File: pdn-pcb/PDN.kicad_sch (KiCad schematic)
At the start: 22 parts, among them CN1 PH-3AW_C722773, CN10 PH-6AW_C722785, CN2 PH-3AW_C722773, CN3 PH-4AW_C722777, CN4 PH-4AW_C722777, CN5 PH-3AW_C722773, CN6 PH-4AW_C722777, CN7 PH-4AW_C722777, CN8 PH-6AW_C722785, CN9 PH-3AW_C722773

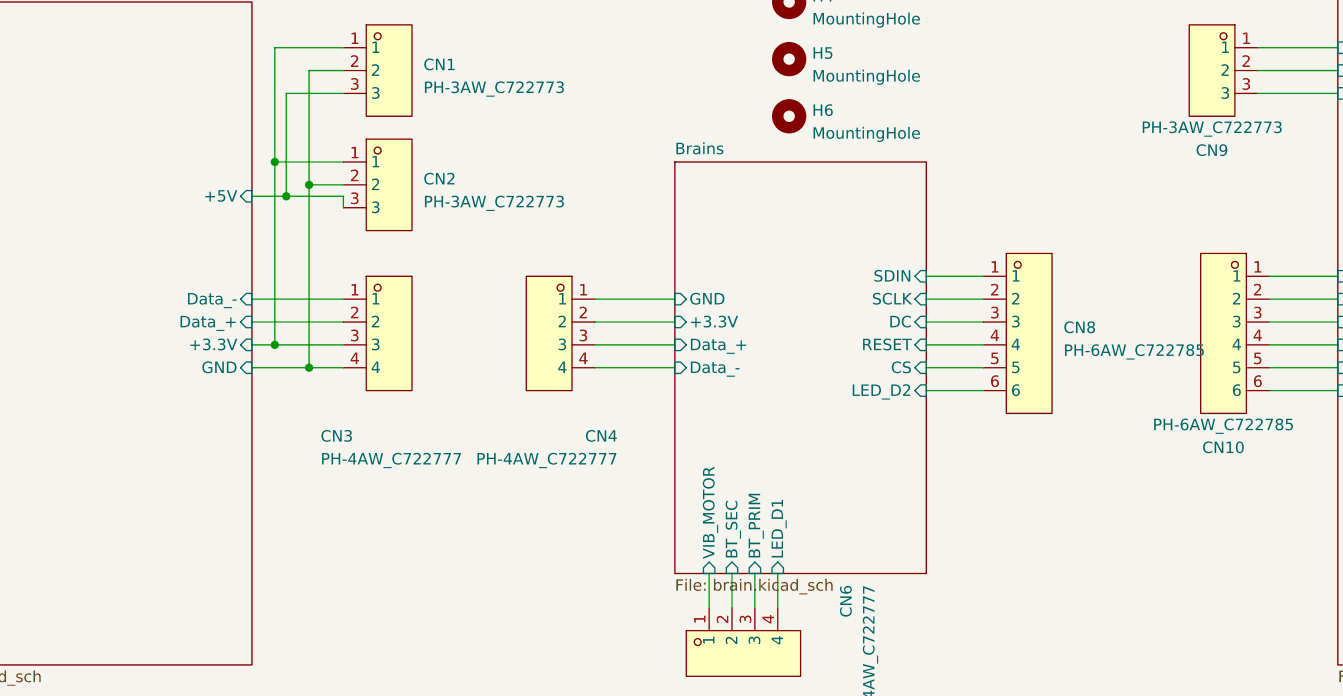
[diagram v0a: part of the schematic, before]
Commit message: Updated 3v3 LDO to an LDL1117, reworked the brain board and added TVS protection.
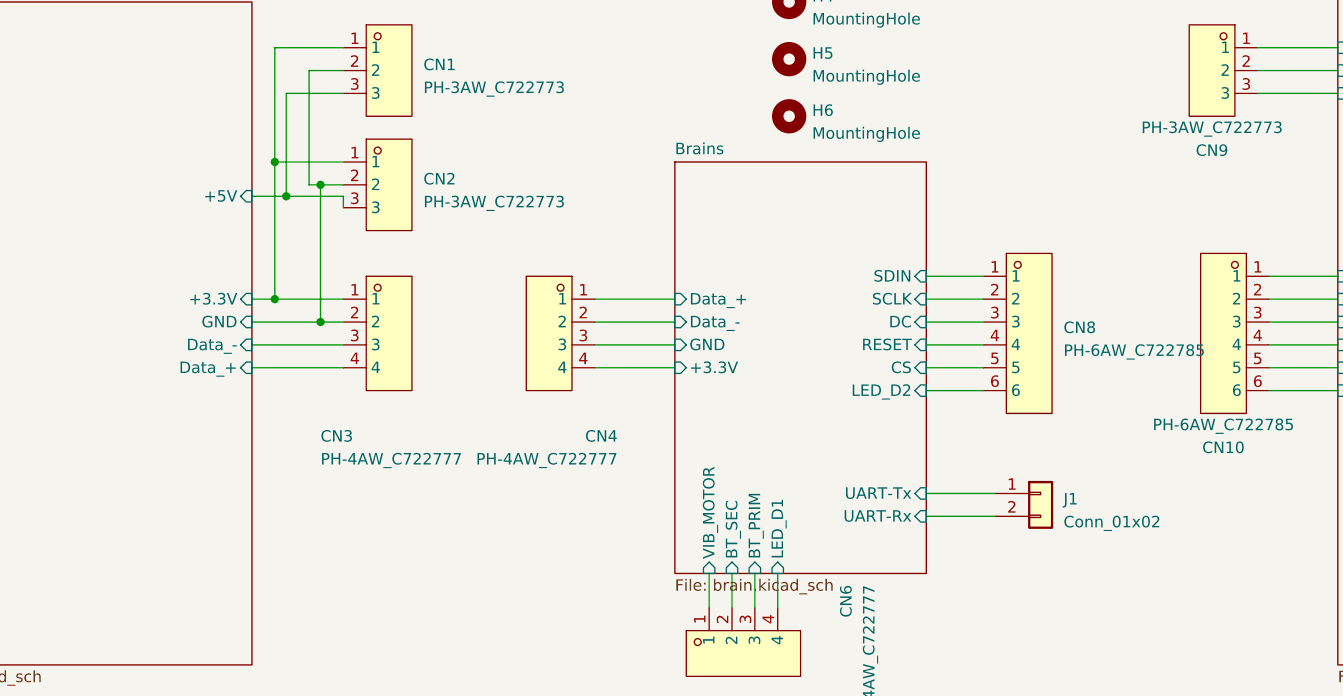
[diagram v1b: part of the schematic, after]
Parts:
- added J1: Conn_01x02, Connector_PinHeader_2.54mm:PinHeader_1x02_P2.54mm_Vertical, symbol Connector_Generic:Conn_01x02
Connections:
- net Brains/+3.3V: now also CN4.4; no longer CN4.2
- net Brains/Data_+: now also CN4.1; no longer CN4.3
- net Brains/Data_-: now also CN4.2; no longer CN4.4
- net Brains/GND: now also CN4.3; no longer CN4.1
- net Power Sheet/+3.3V: now also CN3.1; no longer CN3.3
- net Power Sheet/Data_+: now also CN3.4; no longer CN3.2
- net Power Sheet/Data_-: now also CN3.3; no longer CN3.1
- net Power Sheet/GND: now also CN3.2; no longer CN3.4
- new net Brains/UART-Rx: J1.2 (Pin_2)
- new net Brains/UART-Tx: J1.1 (Pin_1)
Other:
- sheet Brains ports: added UART-Rx, UART-Tx; removed none
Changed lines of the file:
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@@
 (kicad_sch (version 20230121) (generator eeschema)
   (paper "A4")
-  (junction (at 88.9 85.09) (diameter 0) (color 0 0 0 0)
-  )
-  (junction (at 88.9 64.77) (diameter 0) (color 0 0 0 0)
-  )
-  (junction (at 85.09 82.55) (diameter 0) (color 0 0 0 0)
+  (junction (at 85.09 62.23) (diameter 0) (color 0 0 0 0)
+  )
+  (junction (at 90.17 80.01) (diameter 0) (color 0 0 0 0)
   )
   (junction (at 86.36 66.04) (diameter 0) (color 0 0 0 0)
   )
-  (junction (at 85.09 62.23) (diameter 0) (color 0 0 0 0)
+  (junction (at 90.17 64.77) (diameter 0) (color 0 0 0 0)
+  )
+  (junction (at 85.09 77.47) (diameter 0) (color 0 0 0 0)
   )
   (wire (pts (xy 195.58 82.55) (xy 203.2 82.55))
@@
     (stroke (width 0) (type default))
   )
-  (wire (pts (xy 82.55 82.55) (xy 85.09 82.55))
-    (stroke (width 0) (type default))
-  )
-  (wire (pts (xy 88.9 64.77) (xy 92.71 64.77))
+  (wire (pts (xy 85.09 62.23) (xy 85.09 77.47))
+    (stroke (width 0) (type default))
+  )
+  (wire (pts (xy 82.55 82.55) (xy 92.71 82.55))
+    (stroke (width 0) (type default))
+  )
+  (wire (pts (xy 88.9 64.77) (xy 90.17 64.77))
     (stroke (width 0) (type default))
   )
@@
     (stroke (width 0) (type default))
   )
-  (wire (pts (xy 82.55 80.01) (xy 92.71 80.01))
+  (wire (pts (xy 82.55 80.01) (xy 90.17 80.01))
     (stroke (width 0) (type default))
   )
@@
     (stroke (width 0) (type default))
   )
-  (wire (pts (xy 88.9 64.77) (xy 88.9 85.09))
-    (stroke (width 0) (type default))
-  )
   (wire (pts (xy 135.89 107.95) (xy 135.89 111.76))
     (stroke (width 0) (type default))
@@
     (stroke (width 0) (type default))
   )
+  (wire (pts (xy 90.17 64.77) (xy 92.71 64.77))
+    (stroke (width 0) (type default))
+  )
   (wire (pts (xy 195.58 74.93) (xy 203.2 74.93))
     (stroke (width 0) (type default))
@@
     (stroke (width 0) (type default))
   )
+  (wire (pts (xy 90.17 64.77) (xy 90.17 80.01))
+    (stroke (width 0) (type default))
+  )
   (wire (pts (xy 120.65 82.55) (xy 129.54 82.55))
     (stroke (width 0) (type default))
@@
     (stroke (width 0) (type default))
   )
-  (wire (pts (xy 85.09 82.55) (xy 85.09 62.23))
-    (stroke (width 0) (type default))
-  )
-  (wire (pts (xy 82.55 85.09) (xy 88.9 85.09))
+  (wire (pts (xy 82.55 85.09) (xy 92.71 85.09))
     (stroke (width 0) (type default))
   )
@@
     (stroke (width 0) (type default))
   )
-  (wire (pts (xy 88.9 85.09) (xy 92.71 85.09))
-    (stroke (width 0) (type default))
-  )
   (wire (pts (xy 138.43 107.95) (xy 138.43 111.76))
     (stroke (width 0) (type default))
@@
     (stroke (width 0) (type default))
   )
+  (wire (pts (xy 85.09 77.47) (xy 92.71 77.47))
+    (stroke (width 0) (type default))
+  )
   (wire (pts (xy 88.9 52.07) (xy 92.71 52.07))
     (stroke (width 0) (type default))
@@
     (stroke (width 0) (type default))
   )
-  (wire (pts (xy 85.09 82.55) (xy 92.71 82.55))
-    (stroke (width 0) (type default))
-  )
   (wire (pts (xy 140.97 107.95) (xy 140.97 111.76))
     (stroke (width 0) (type default))
   )
+  (wire (pts (xy 90.17 80.01) (xy 92.71 80.01))
+    (stroke (width 0) (type default))
+  )
   (wire (pts (xy 195.58 85.09) (xy 203.2 85.09))
     (stroke (width 0) (type default))
   )
+  (wire (pts (xy 157.48 99.06) (xy 165.1 99.06))
+    (stroke (width 0) (type default))
+  )
   (wire (pts (xy 85.09 62.23) (xy 85.09 49.53))
     (stroke (width 0) (type default))
   )
-  (wire (pts (xy 82.55 77.47) (xy 92.71 77.47))
+  (wire (pts (xy 82.55 77.47) (xy 85.09 77.47))
+    (stroke (width 0) (type default))
+  )
+  (wire (pts (xy 157.48 101.6) (xy 165.1 101.6))
     (stroke (width 0) (type default))
   )
@@
         (path "/df0bc267-025e-4c4e-a09b-51ff87d0c1db"
           (reference "CN7") (unit 1)
+        )
+      )
+    )
+  )
+  (symbol (lib_id "Connector_Generic:Conn_01x02") (at 170.18 99.06 0) (unit 1)
+    (in_bom yes) (on_board yes) (dnp no) (fields_autoplaced)
+    (property "Reference" "J1" (at 172.72 99.695 0)
+      (effects (font (size 1.27 1.27)) (justify left))
+    )
+    (property "Value" "Conn_01x02" (at 172.72 102.235 0)
+      (effects (font (size 1.27 1.27)) (justify left))
+    )
+    (property "Footprint" "Connector_PinHeader_2.54mm:PinHeader_1x02_P2.54mm_Vertical" (at 170.18 99.06 0)
+      (effects (font (size 1.27 1.27)) hide)
+    )
+    (property "Datasheet" "~" (at 170.18 99.06 0)
+      (effects (font (size 1.27 1.27)) hide)
+    )
+    (pin "1")
+    (pin "2")
+    (instances
+      (project "PDN"
+        (path "/df0bc267-025e-4c4e-a09b-51ff87d0c1db"
+          (reference "J1") (unit 1)
         )
       )
@@
       (effects (font (size 1.27 1.27)) hide)
     )
-    (pin "GND" input (at 129.54 77.47 180)
-      (effects (font (size 1.27 1.27)) (justify left))
-    )
-    (pin "+3.3V" input (at 129.54 80.01 180)
+    (pin "GND" input (at 129.54 82.55 180)
+      (effects (font (size 1.27 1.27)) (justify left))
+    )
+    (pin "+3.3V" input (at 129.54 85.09 180)
       (effects (font (size 1.27 1.27)) (justify left))
     )
@@
       (effects (font (size 1.27 1.27)) (justify left))
     )
-    (pin "Data_-" input (at 129.54 85.09 180)
-      (effects (font (size 1.27 1.27)) (justify left))
-    )
-    (pin "Data_+" input (at 129.54 82.55 180)
+    (pin "Data_-" input (at 129.54 80.01 180)
+      (effects (font (size 1.27 1.27)) (justify left))
+    )
+    (pin "Data_+" input (at 129.54 77.47 180)
       (effects (font (size 1.27 1.27)) (justify left))
     )
@@
     )
     (pin "LED_D2" input (at 157.48 87.63 0)
+      (effects (font (size 1.27 1.27)) (justify right))
+    )
+    (pin "UART-Rx" input (at 157.48 101.6 0)
+      (effects (font (size 1.27 1.27)) (justify right))
+    )
+    (pin "UART-Tx" input (at 157.48 99.06 0)
       (effects (font (size 1.27 1.27)) (justify right))
     )
@@
       (effects (font (size 1.27 1.27)) hide)
     )
-    (pin "GND" input (at 82.55 85.09 0)
+    (pin "GND" input (at 82.55 80.01 0)
       (effects (font (size 1.27 1.27)) (justify right))
     )
@@
       (effects (font (size 1.27 1.27)) (justify right))
     )
-    (pin "+3.3V" input (at 82.55 82.55 0)
-      (effects (font (size 1.27 1.27)) (justify right))
-    )
-    (pin "Data_+" input (at 82.55 80.01 0)
-      (effects (font (size 1.27 1.27)) (justify right))
-    )
-    (pin "Data_-" input (at 82.55 77.47 0)
-      (effects (font (size 1.27 1.27)) (justify right))
-    )
+    (pin "+3.3V" input (at 82.55 77.47 0)
+      (effects (font (size 1.27 1.27)) (justify right))
+    )
+    (pin "Data_+" input (at 82.55 85.09 0)
+      (effects (font (size 1.27 1.27)) (justify right))
+    )
+    (pin "Data_-" input (at 82.55 82.55 0)
+      (effects (font (size 1.27 1.27)) (justify right))
+    )
